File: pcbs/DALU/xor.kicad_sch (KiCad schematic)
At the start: 6 parts, among them U601 74HC86, U602 74HC86, U603 74HC245

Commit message: More rerouting
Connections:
- net RESULT7: now reaches U603.11 (B7)
- net RESULT6: now reaches U603.12 (B6)
- net RESULT5: now reaches U603.13 (B5)
- net RESULT4: now reaches U603.14 (B4)
- net RESULT3: now reaches U603.15 (B3)
- net RESULT2: now reaches U603.16 (B2)
- net RESULT1: now reaches U603.17 (B1)
- net RESULT0: now reaches U603.18 (B0)
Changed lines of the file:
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@@
+    (stroke (width 0) (type default) (color 0 0 0 0))
+  )
+  (bus_entry (at 244.475 57.15) (size -2.54 2.54)
+    (stroke (width 0) (type default) (color 0 0 0 0))
+  )
+  (bus_entry (at 244.475 59.69) (size -2.54 2.54)
     (stroke (width 0) (type default) (color 0 0 0 0))
   )
@@
     (stroke (width 0) (type default) (color 0 0 0 0))
   )
+  (bus_entry (at 244.475 54.61) (size -2.54 2.54)
+    (stroke (width 0) (type default) (color 0 0 0 0))
+  )
+  (bus_entry (at 244.475 41.91) (size -2.54 2.54)
+    (stroke (width 0) (type default) (color 0 0 0 0))
+  )
   (bus_entry (at 88.9 53.34) (size 2.54 2.54)
     (stroke (width 0) (type default) (color 0 0 0 0))
   )
+  (bus_entry (at 244.475 46.99) (size -2.54 2.54)
+    (stroke (width 0) (type default) (color 0 0 0 0))
+  )
   (bus_entry (at 83.82 143.51) (size 2.54 2.54)
     (stroke (width 0) (type default) (color 0 0 0 0))
   )
+  (bus_entry (at 244.475 49.53) (size -2.54 2.54)
+    (stroke (width 0) (type default) (color 0 0 0 0))
+  )
   (bus_entry (at 88.9 96.52) (size 2.54 2.54)
     (stroke (width 0) (type default) (color 0 0 0 0))
@@
     (stroke (width 0) (type default) (color 0 0 0 0))
   )
+  (bus_entry (at 244.475 44.45) (size -2.54 2.54)
+    (stroke (width 0) (type default) (color 0 0 0 0))
+  )
+  (bus_entry (at 244.475 52.07) (size -2.54 2.54)
+    (stroke (width 0) (type default) (color 0 0 0 0))
+  )
   (bus_entry (at 88.9 39.37) (size 2.54 2.54)
     (stroke (width 0) (type default) (color 0 0 0 0))
@@
     (stroke (width 0) (type default) (color 0 0 0 0))
   )
+  (wire (pts (xy 228.6 46.99) (xy 241.935 46.99))
+    (stroke (width 0) (type default) (color 0 0 0 0))
+  )
   (wire (pts (xy 130.81 115.57) (xy 116.84 115.57))
     (stroke (width 0) (type default) (color 0 0 0 0))
@@
     (stroke (width 0) (type default) (color 0 0 0 0))
   )
+  (bus (pts (xy 244.475 41.91) (xy 244.475 44.45))
+    (stroke (width 0) (type default) (color 0 0 0 0))
+  )
   (wire (pts (xy 91.44 69.85) (xy 101.6 69.85))
     (stroke (width 0) (type default) (color 0 0 0 0))
@@
     (stroke (width 0) (type default) (color 0 0 0 0))
   )
+  (wire (pts (xy 228.6 57.15) (xy 241.935 57.15))
+    (stroke (width 0) (type default) (color 0 0 0 0))
+  )
   (wire (pts (xy 91.44 140.97) (xy 101.6 140.97))
     (stroke (width 0) (type default) (color 0 0 0 0))
@@
     (stroke (width 0) (type default) (color 0 0 0 0))
   )
+  (wire (pts (xy 228.6 59.69) (xy 241.935 59.69))
+    (stroke (width 0) (type default) (color 0 0 0 0))
+  )
   (wire (pts (xy 128.27 101.6) (xy 116.84 101.6))
     (stroke (width 0) (type default) (color 0 0 0 0))
@@
     (stroke (width 0) (type default) (color 0 0 0 0))
   )
+  (bus (pts (xy 244.475 54.61) (xy 244.475 57.15))
+    (stroke (width 0) (type default) (color 0 0 0 0))
+  )
   (wire (pts (xy 184.785 124.46) (xy 191.77 124.46))
     (stroke (width 0) (type default) (color 0 0 0 0))
@@
     (stroke (width 0) (type default) (color 0 0 0 0))
   )
+  (bus (pts (xy 244.475 35.56) (xy 244.475 41.91))
+    (stroke (width 0) (type default) (color 0 0 0 0))
+  )
   (bus (pts (xy 83.82 86.36) (xy 83.82 101.6))
     (stroke (width 0) (type default) (color 0 0 0 0))
@@
     (stroke (width 0) (type default) (color 0 0 0 0))
   )
+  (wire (pts (xy 228.6 62.23) (xy 241.935 62.23))
+    (stroke (width 0) (type default) (color 0 0 0 0))
+  )
   (bus (pts (xy 88.9 25.4) (xy 88.9 39.37))
     (stroke (width 0) (type default) (color 0 0 0 0))
@@
     (stroke (width 0) (type default) (color 0 0 0 0))
   )
+  (bus (pts (xy 244.475 49.53) (xy 244.475 52.07))
+    (stroke (width 0) (type default) (color 0 0 0 0))
+  )
   (bus (pts (xy 88.9 39.37) (xy 88.9 53.34))
     (stroke (width 0) (type default) (color 0 0 0 0))
   )
+  (bus (pts (xy 251.46 35.56) (xy 244.475 35.56))
+    (stroke (width 0) (type default) (color 0 0 0 0))
+  )
   (wire (pts (xy 116.84 44.45) (xy 203.2 44.45))
     (stroke (width 0) (type default) (color 0 0 0 0))
@@
     (stroke (width 0) (type default) (color 0 0 0 0))
   )
+  (wire (pts (xy 228.6 49.53) (xy 241.935 49.53))
+    (stroke (width 0) (type default) (color 0 0 0 0))
+  )
   (wire (pts (xy 203.2 62.23) (xy 135.89 62.23))
     (stroke (width 0) (type default) (color 0 0 0 0))
@@
     (stroke (width 0) (type default) (color 0 0 0 0))
   )
+  (wire (pts (xy 228.6 44.45) (xy 241.935 44.45))
+    (stroke (width 0) (type default) (color 0 0 0 0))
+  )
   (wire (pts (xy 203.2 49.53) (xy 123.19 49.53))
     (stroke (width 0) (type default) (color 0 0 0 0))
@@
     (stroke (width 0) (type default) (color 0 0 0 0))
   )
+  (bus (pts (xy 244.475 57.15) (xy 244.475 59.69))
+    (stroke (width 0) (type default) (color 0 0 0 0))
+  )
   (wire (pts (xy 179.705 135.255) (xy 179.705 136.525))
     (stroke (width 0) (type default) (color 0 0 0 0))
@@
     (stroke (width 0) (type default) (color 0 0 0 0))
   )
+  (bus (pts (xy 244.475 52.07) (xy 244.475 54.61))
+    (stroke (width 0) (type default) (color 0 0 0 0))
+  )
   (wire (pts (xy 191.77 124.46) (xy 205.105 124.46))
     (stroke (width 0) (type default) (color 0 0 0 0))
@@
     (stroke (width 0) (type default) (color 0 0 0 0))
   )
+  (bus (pts (xy 244.475 46.99) (xy 244.475 49.53))
+    (stroke (width 0) (type default) (color 0 0 0 0))
+  )
   (wire (pts (xy 125.73 52.07) (xy 203.2 52.07))
     (stroke (width 0) (type default) (color 0 0 0 0))
@@
     (stroke (width 0) (type default) (color 0 0 0 0))
   )
+  (wire (pts (xy 228.6 52.07) (xy 241.935 52.07))
+    (stroke (width 0) (type default) (color 0 0 0 0))
+  )
   (wire (pts (xy 135.89 143.51) (xy 116.84 143.51))
     (stroke (width 0) (type default) (color 0 0 0 0))
@@
     (stroke (width 0) (type default) (color 0 0 0 0))
   )
+  (wire (pts (xy 228.6 54.61) (xy 241.935 54.61))
+    (stroke (width 0) (type default) (color 0 0 0 0))
+  )
   (wire (pts (xy 91.44 55.88) (xy 101.6 55.88))
     (stroke (width 0) (type default) (color 0 0 0 0))
@@
     (stroke (width 0) (type default) (color 0 0 0 0))
   )
+  (bus (pts (xy 244.475 44.45) (xy 244.475 46.99))
+    (stroke (width 0) (type default) (color 0 0 0 0))
+  )
   (wire (pts (xy 196.215 69.85) (xy 203.2 69.85))
     (stroke (width 0) (type default) (color 0 0 0 0))
@@
     (stroke (width 0) (type default) (color 0 0 0 0))
   )
+  (label "RESULT0" (at 228.6 44.45 0)
+    (effects (font (size 1.27 1.27)) (justify left bottom))
+  )
   (label "XOR5" (at 143.51 57.15 0)
     (effects (font (size 1.27 1.27)) (justify left bottom))
@@
     (effects (font (size 1.27 1.27)) (justify left bottom))
   )
+  (label "RESULT7" (at 228.6 62.23 0)
+    (effects (font (size 1.27 1.27)) (justify left bottom))
+  )
+  (label "RESULT2" (at 228.6 49.53 0)
+    (effects (font (size 1.27 1.27)) (justify left bottom))
+  )
   (label "B0" (at 91.44 46.99 0)
     (effects (font (size 1.27 1.27)) (justify left bottom))
@@
     (effects (font (size 1.27 1.27)) (justify left bottom))
   )
+  (label "RESULT6" (at 228.6 59.69 0)
+    (effects (font (size 1.27 1.27)) (justify left bottom))
+  )
+  (label "RESULT5" (at 228.6 57.15 0)
+    (effects (font (size 1.27 1.27)) (justify left bottom))
+  )
   (label "B4" (at 91.44 104.14 0)
     (effects (font (size 1.27 1.27)) (justify left bottom))
   )
+  (label "RESULT1" (at 228.6 46.99 0)
+    (effects (font (size 1.27 1.27)) (justify left bottom))
+  )
+  (label "RESULT3" (at 228.6 52.07 0)
+    (effects (font (size 1.27 1.27)) (justify left bottom))
+  )
   (label "XOR1" (at 143.51 46.99 0)
     (effects (font (size 1.27 1.27)) (justify left bottom))
   )
   (label "XOR2" (at 143.51 49.53 0)
+    (effects (font (size 1.27 1.27)) (justify left bottom))
+  )
+  (label "RESULT4" (at 228.6 54.61 0)
     (effects (font (size 1.27 1.27)) (justify left bottom))
   )
@@
     (effects (font (size 1.27 1.27)) (justify right))
   )
+  (hierarchical_label "RESULT[0..7]" (shape tri_state) (at 251.46 35.56 0)
+    (effects (font (size 1.27 1.27)) (justify left))
+  )
   (hierarchical_label "~{XOR}" (shape input) (at 195.58 69.85 180)

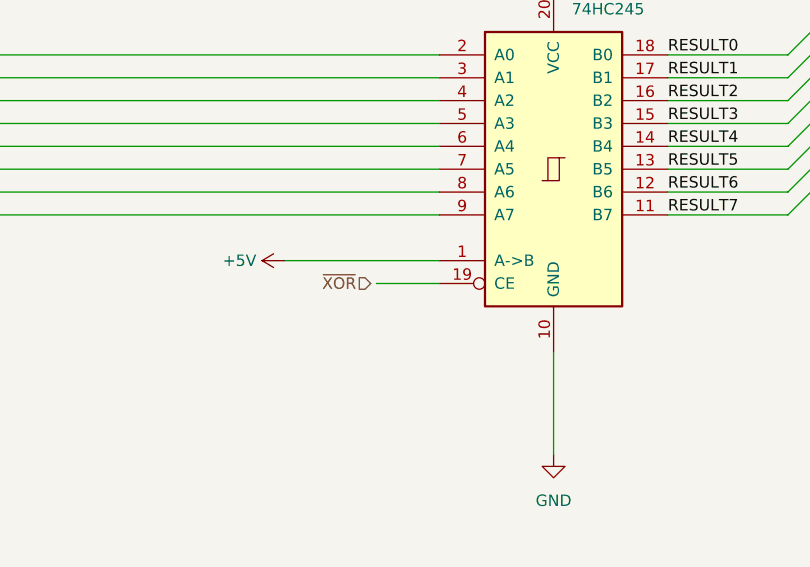
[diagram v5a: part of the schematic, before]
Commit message: Starting to connect up control wires
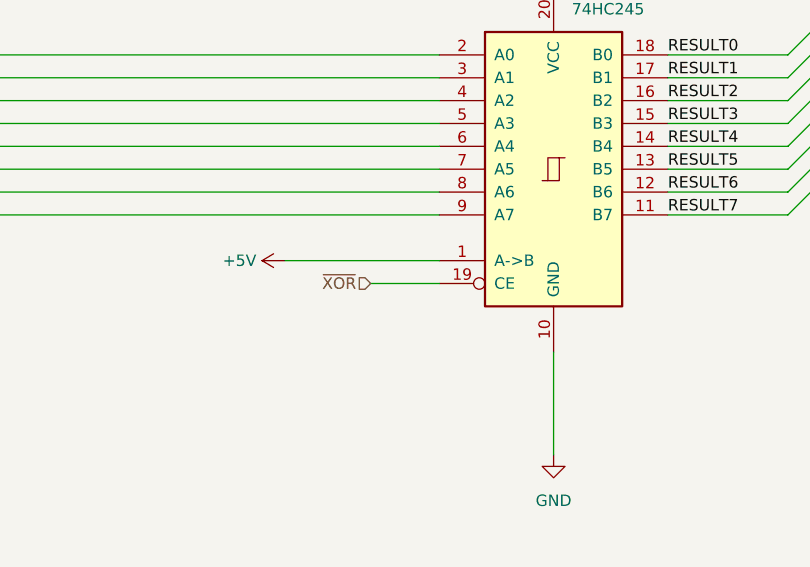
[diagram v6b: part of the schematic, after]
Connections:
- net ~{XOR}: now also U603.19 (CE)
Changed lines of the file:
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@@
+    (stroke (width 0) (type default) (color 0 0 0 0))
+  )
+  (wire (pts (xy 195.58 69.85) (xy 203.2 69.85))
     (stroke (width 0) (type default) (color 0 0 0 0))
   )
@@
     (stroke (width 0) (type default) (color 0 0 0 0))
   )
-  (wire (pts (xy 196.215 69.85) (xy 203.2 69.85))
-    (stroke (width 0) (type default) (color 0 0 0 0))
-  )

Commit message: Sending for production
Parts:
- U601, U602: now left out of the parts list
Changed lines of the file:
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@@
   )
   (symbol (lib_id "74xx:74HC86") (at 57.15 171.45 0) (unit 5)
-    (in_bom yes) (on_board yes) (fields_autoplaced)
+    (in_bom no) (on_board yes) (fields_autoplaced)
     (property "Reference" "U602" (id 0) (at 63.5 170.1799 0)
       (effects (font (size 1.27 1.27)) (justify left))
@@
   )
   (symbol (lib_id "74xx:74HC86") (at 109.22 72.39 0) (unit 1)
-    (in_bom yes) (on_board yes) (fields_autoplaced)
+    (in_bom no) (on_board yes) (fields_autoplaced)
     (property "Reference" "U601" (id 0) (at 108.9152 63.5 0))
     (property "Value" "74HC86" (id 1) (at 108.9152 66.04 0))
@@
   )
   (symbol (lib_id "74xx:74HC86") (at 109.22 115.57 0) (unit 2)
-    (in_bom yes) (on_board yes) (fields_autoplaced)
+    (in_bom no) (on_board yes) (fields_autoplaced)
     (property "Reference" "U602" (id 0) (at 108.9152 106.68 0))
     (property "Value" "74HC86" (id 1) (at 108.9152 109.22 0))
@@
   )
   (symbol (lib_id "74xx:74HC86") (at 109.22 129.54 0) (unit 3)
-    (in_bom yes) (on_board yes) (fields_autoplaced)
+    (in_bom no) (on_board yes) (fields_autoplaced)
     (property "Reference" "U602" (id 0) (at 108.9152 120.65 0))
     (property "Value" "74HC86" (id 1) (at 108.9152 123.19 0))
@@
   )
   (symbol (lib_id "74xx:74HC86") (at 109.22 44.45 0) (unit 3)
-    (in_bom yes) (on_board yes) (fields_autoplaced)
+    (in_bom no) (on_board yes) (fields_autoplaced)
     (property "Reference" "U601" (id 0) (at 108.9152 35.56 0))
     (property "Value" "74HC86" (id 1) (at 108.9152 38.1 0))
@@
   )
   (symbol (lib_id "74xx:74HC86") (at 109.22 143.51 0) (unit 4)
-    (in_bom yes) (on_board yes) (fields_autoplaced)
+    (in_bom no) (on_board yes) (fields_autoplaced)
     (property "Reference" "U602" (id 0) (at 108.9152 134.62 0))
     (property "Value" "74HC86" (id 1) (at 108.9152 137.16 0))
@@
   )
   (symbol (lib_id "74xx:74HC86") (at 109.22 101.6 0) (unit 1)
-    (in_bom yes) (on_board yes) (fields_autoplaced)
+    (in_bom no) (on_board yes) (fields_autoplaced)
     (property "Reference" "U602" (id 0) (at 108.9152 92.71 0))
     (property "Value" "74HC86" (id 1) (at 108.9152 95.25 0))
@@
   )
   (symbol (lib_id "74xx:74HC86") (at 109.22 58.42 0) (unit 4)
-    (in_bom yes) (on_board yes) (fields_autoplaced)
+    (in_bom no) (on_board yes) (fields_autoplaced)
     (property "Reference" "U601" (id 0) (at 108.9152 49.53 0))
     (property "Value" "74HC86" (id 1) (at 108.9152 52.07 0))
@@
   )
   (symbol (lib_id "74xx:74HC86") (at 29.21 171.45 0) (unit 5)
-    (in_bom yes) (on_board yes) (fields_autoplaced)
+    (in_bom no) (on_board yes) (fields_autoplaced)
     (property "Reference" "U601" (id 0) (at 35.56 170.1799 0)
       (effects (font (size 1.27 1.27)) (justify left))
@@
   )
   (symbol (lib_id "74xx:74HC86") (at 109.22 86.36 0) (unit 2)
-    (in_bom yes) (on_board yes) (fields_autoplaced)
+    (in_bom no) (on_board yes) (fields_autoplaced)
     (property "Reference" "U601" (id 0) (at 108.9152 77.47 0))
     (property "Value" "74HC86" (id 1) (at 108.9152 80.01 0))
